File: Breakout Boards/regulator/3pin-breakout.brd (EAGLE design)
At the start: 19.1 x 16.5 mm, 17 parts

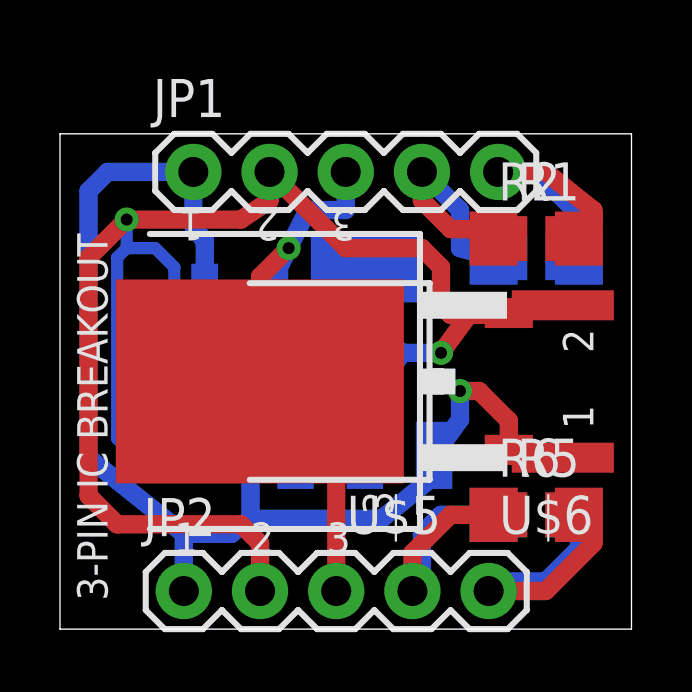
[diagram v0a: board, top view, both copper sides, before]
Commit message: new prototype for dual tube board
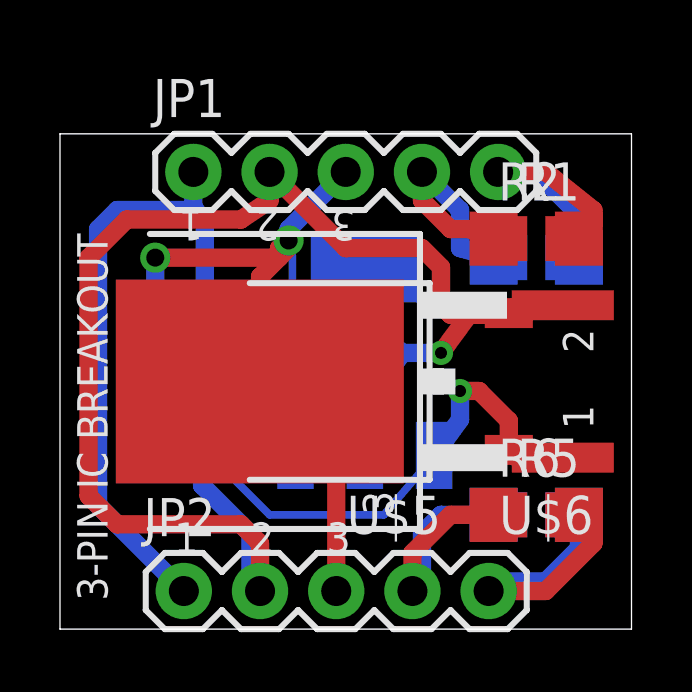
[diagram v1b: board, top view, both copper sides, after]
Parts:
- moved U$3 2.22 mm to (3.81, 8.89)
- moved U$4 2.22 mm to (3.81, 8.89)
- moved U$1 1.90 mm to (3.81, 8.89)
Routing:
- net N$2: track 63.8 -> 57.1 mm, vias 2 -> 1
- net N$1: track 45.4 -> 44.6 mm
- net N$3: track 34.3 -> 33.9 mm, vias 1 -> 2
